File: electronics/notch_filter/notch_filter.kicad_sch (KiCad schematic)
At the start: 32 parts, among them J1 Conn_01x03, J2 Conn_01x03, J3 Output, J4 In, J5 module_2x15_left_input, J6 module_2x15_right_input, U1 opamp_single_8pin

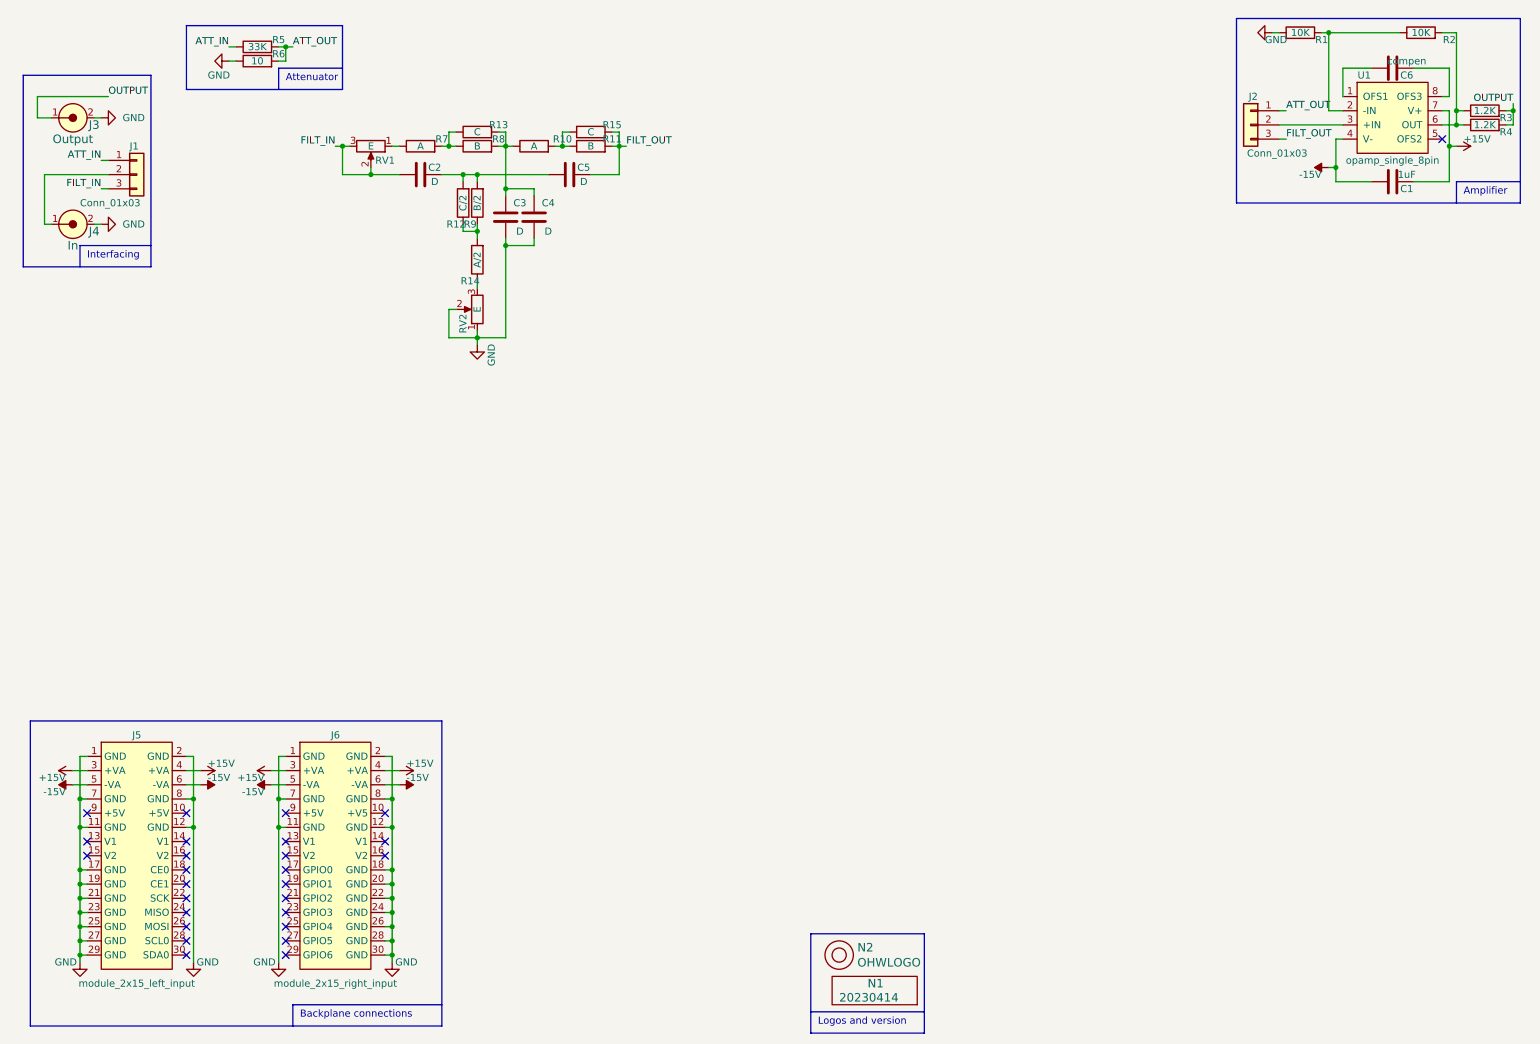
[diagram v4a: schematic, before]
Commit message: footprint changes, changed power rails, silk placed, added labels, increased size of labels
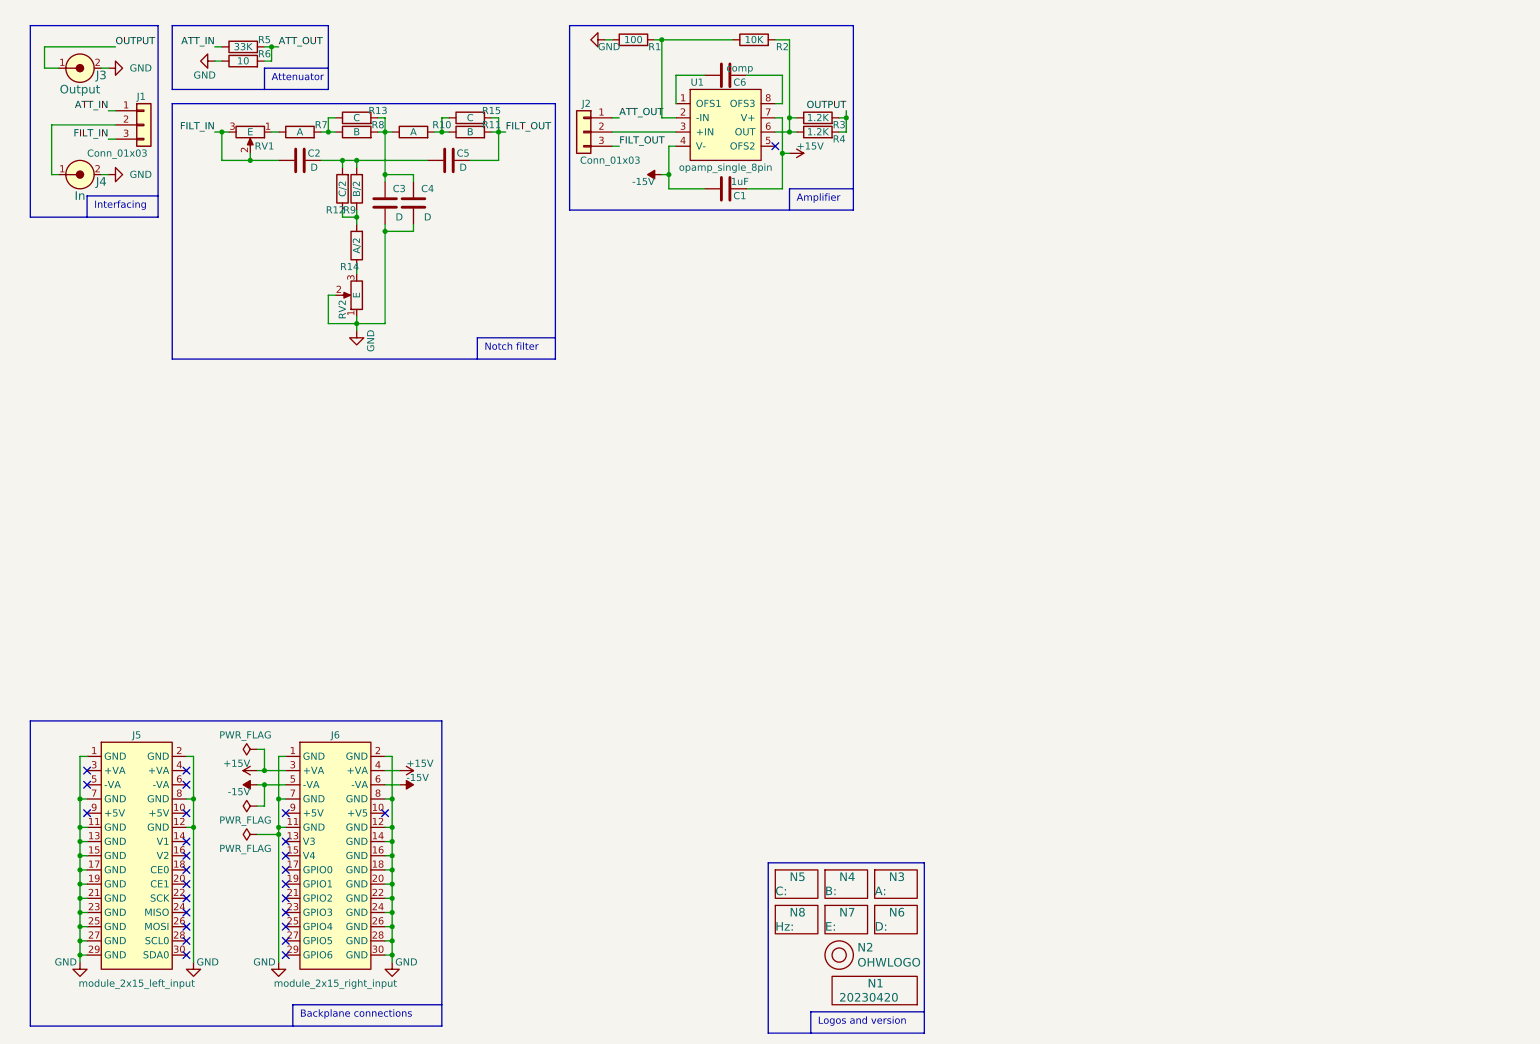
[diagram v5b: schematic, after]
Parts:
- added N3: A:, SquantorLabels:Label_Note_medium, symbol SquantorLabels:Label
- added N4: B:, SquantorLabels:Label_Note_medium, symbol SquantorLabels:Label
- added N5: C:, SquantorLabels:Label_Note_medium, symbol SquantorLabels:Label
- added N6: D:, SquantorLabels:Label_Note_medium, symbol SquantorLabels:Label
- added N7: E:, SquantorLabels:Label_Note_medium, symbol SquantorLabels:Label
- added N8: Hz:, SquantorLabels:Label_Note_medium, symbol SquantorLabels:Label
- C2, C3, C4, C5: footprint SquantorRcl:C-025_050-050X100-film -> SquantorRcl:C-025_050-050X100-0805-3516-film
- C6: value compen -> comp
- N1: value 20230414 -> 20230420
- R1: value 10K -> 100
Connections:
- net +15V: no longer J5.3 (+VA), J5.4 (+VA)
- net -15V: no longer J5.5 (-VA), J5.6 (-VA)
- net GND: now also J5.13 (GND), J5.15 (GND), J6.14 (GND), J6.16 (GND)
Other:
- note added: "Notch filter"
- moved on the sheet: C1, C2, C3, C4, C5, C6, J1, J2, J3, J4, R1, R10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

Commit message: added 1M input resistor
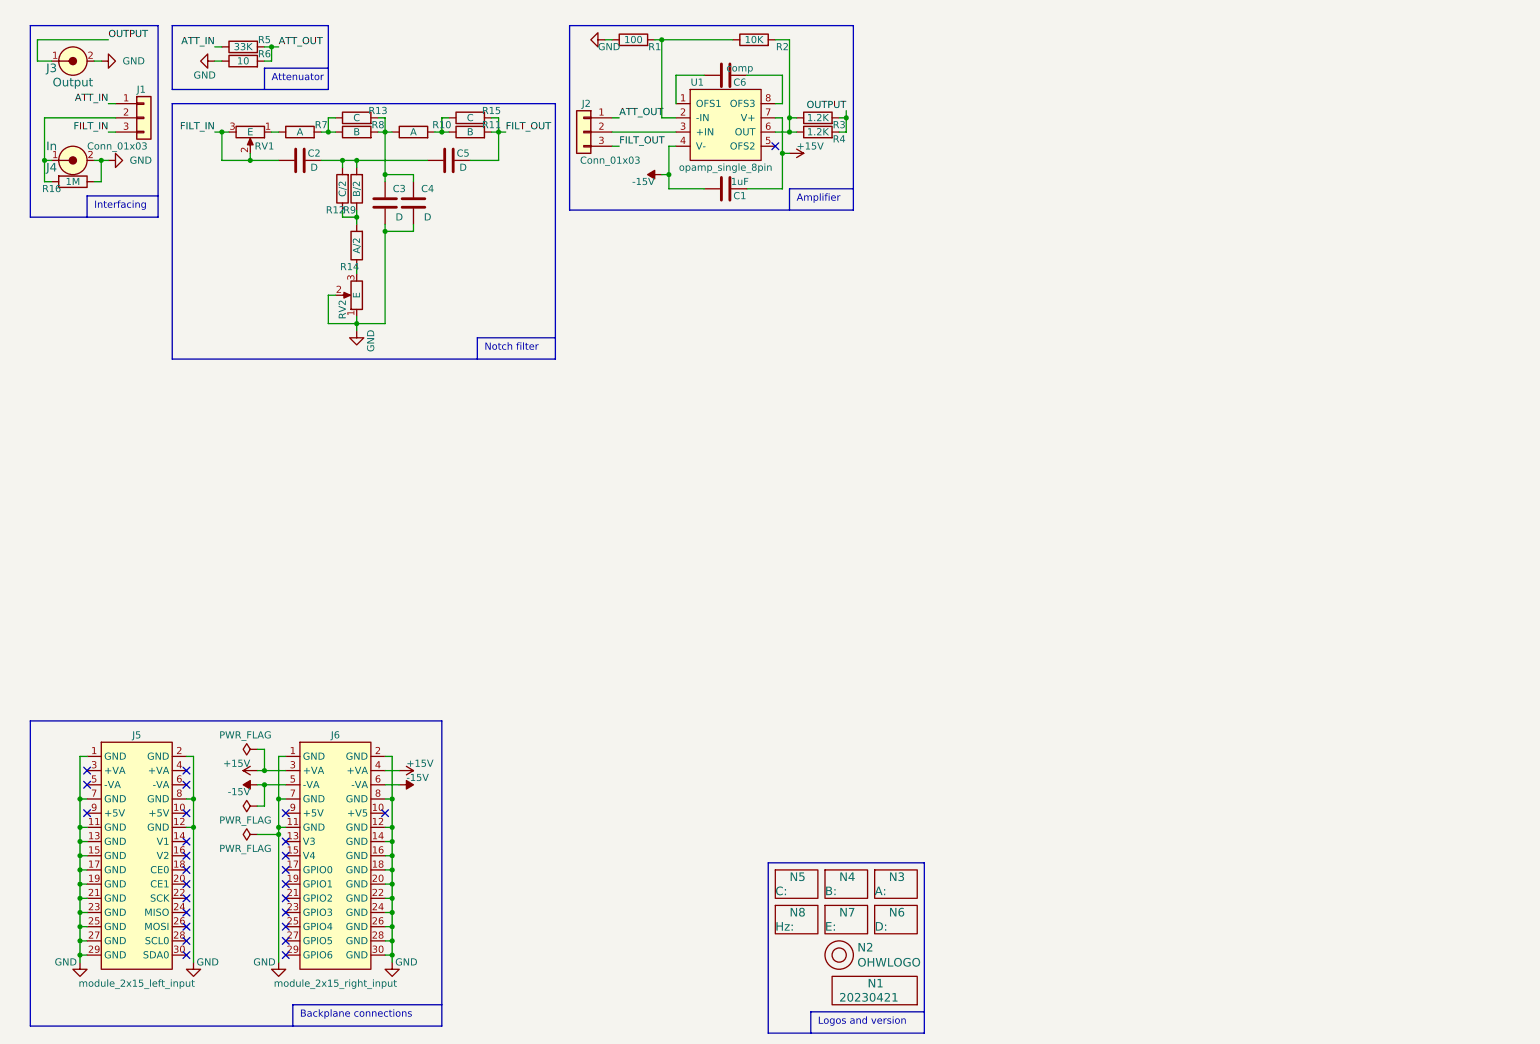
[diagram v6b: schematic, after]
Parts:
- added R16: 1M, SquantorRcl:R_0805+0603, symbol Device:R
- N1: value 20230420 -> 20230421
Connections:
- net GND: now also R16.1
- net at J1.2 (Pin_2), J4.1: now also R16.2
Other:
- moved on the sheet: J1, J3, J4

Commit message: ERC/DRC passes, small ergonomic changes
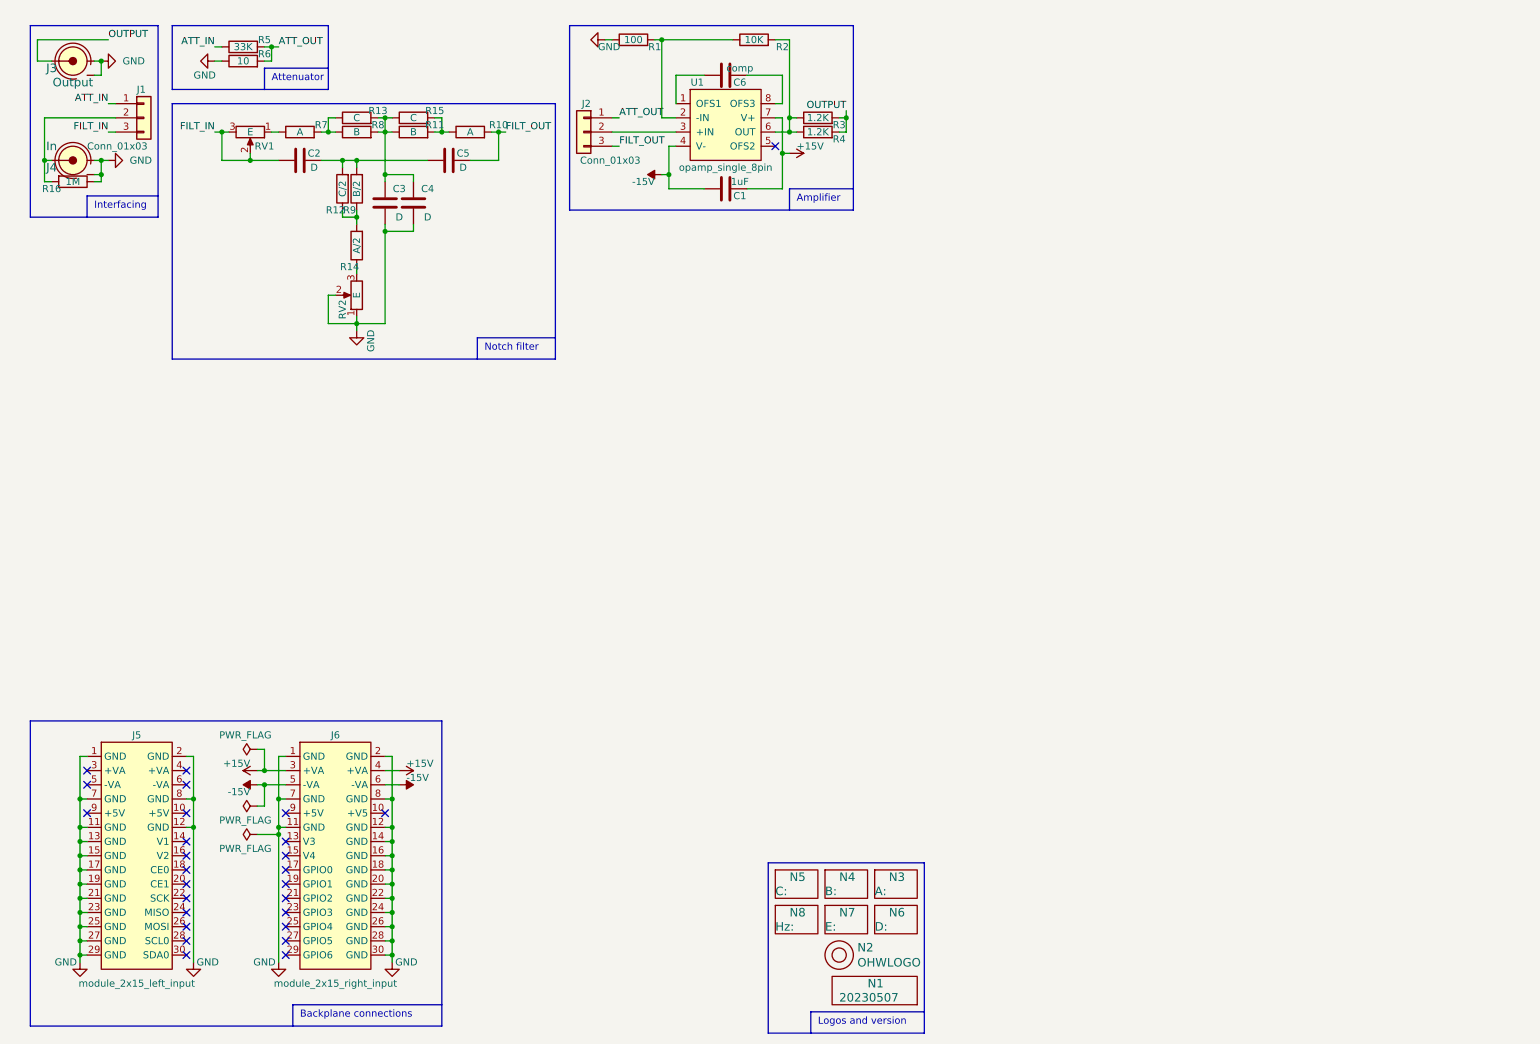
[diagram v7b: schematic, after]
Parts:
- J3, J4: symbol SquantorConnectors:Coax -> SquantorConnectors:Coax_shielded
- N1: value 20230421 -> 20230507
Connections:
- net FILT_OUT: now also R10.2; no longer R11.2, R15.2
- net GND: now also J3.S, J4.S
- net at C3.2, C4.2, R13.2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: now also R11.1, R15.1; no longer R10.1
- new net: R10.1, R11.2, R15.2
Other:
- moved on the sheet: R10, R11, R15
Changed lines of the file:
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@@
   (junction (at 24.13 179.07) (diameter 0) (color 0 0 0 0)
   )
+  (junction (at 78.74 31.75) (diameter 0) (color 0 0 0 0)
+  )
   (junction (at 80.01 181.61) (diameter 0) (color 0 0 0 0)
   )
@@
   (junction (at 17.78 39.37) (diameter 0) (color 0 0 0 0)
   )
+  (junction (at 27.94 41.91) (diameter 0) (color 0 0 0 0)
+  )
   (junction (at 24.13 161.29) (diameter 0) (color 0 0 0 0)
   )
@@
   )
   (junction (at 73.66 68.58) (diameter 0) (color 0 0 0 0)
+  )
+  (junction (at 27.94 21.59) (diameter 0) (color 0 0 0 0)
   )
   (junction (at 68.58 34.29) (diameter 0) (color 0 0 0 0)
@@
     (stroke (width 0) (type default) (color 0 0 0 0))
   )
+  (wire (pts (xy 27.94 21.59) (xy 27.94 24.13))
+    (stroke (width 0) (type default) (color 0 0 0 0))
+  )
   (wire (pts (xy 59.69 153.67) (xy 60.96 153.67))
     (stroke (width 0) (type default) (color 0 0 0 0))
@@
     (stroke (width 0) (type default) (color 0 0 0 0))
   )
-  (wire (pts (xy 27.94 43.18) (xy 27.94 39.37))
+  (wire (pts (xy 27.94 43.18) (xy 27.94 41.91))
     (stroke (width 0) (type default) (color 0 0 0 0))
   )
@@
     (stroke (width 0) (type default) (color 0 0 0 0))
   )
-  (wire (pts (xy 99.06 31.75) (xy 99.06 34.29))
-    (stroke (width 0) (type default) (color 0 0 0 0))
-  )
   (polyline (pts (xy 162.56 15.24) (xy 111.76 15.24))
     (stroke (width 0) (type default) (color 0 0 0 0))
@@
     (stroke (width 0) (type default) (color 0 0 0 0))
   )
+  (wire (pts (xy 78.74 31.75) (xy 80.01 31.75))
+    (stroke (width 0) (type default) (color 0 0 0 0))
+  )
   (wire (pts (xy 83.82 41.91) (xy 78.74 41.91))
     (stroke (width 0) (type default) (color 0 0 0 0))
@@
     (stroke (width 0) (type default) (color 0 0 0 0))
   )
-  (wire (pts (xy 90.17 31.75) (xy 88.9 31.75))
+  (wire (pts (xy 87.63 31.75) (xy 88.9 31.75))
     (stroke (width 0) (type default) (color 0 0 0 0))
   )
@@
     (stroke (width 0) (type default) (color 0 0 0 0))
   )
-  (wire (pts (xy 97.79 31.75) (xy 99.06 31.75))
-    (stroke (width 0) (type default) (color 0 0 0 0))
-  )
   (wire (pts (xy 80.01 168.91) (xy 80.01 171.45))
     (stroke (width 0) (type default) (color 0 0 0 0))
@@
     (stroke (width 0) (type default) (color 0 0 0 0))
   )
+  (wire (pts (xy 27.94 41.91) (xy 27.94 39.37))
+    (stroke (width 0) (type default) (color 0 0 0 0))
+  )
   (wire (pts (xy 97.79 34.29) (xy 99.06 34.29))
     (stroke (width 0) (type default) (color 0 0 0 0))
@@
     (stroke (width 0) (type default) (color 0 0 0 0))
   )
+  (wire (pts (xy 27.94 24.13) (xy 26.67 24.13))
+    (stroke (width 0) (type default) (color 0 0 0 0))
+  )
   (wire (pts (xy 49.53 39.37) (xy 49.53 34.29))
     (stroke (width 0) (type default) (color 0 0 0 0))
@@
   )
   (wire (pts (xy 24.13 173.99) (xy 24.13 176.53))
+    (stroke (width 0) (type default) (color 0 0 0 0))
+  )
+  (wire (pts (xy 26.67 41.91) (xy 27.94 41.91))
     (stroke (width 0) (type default) (color 0 0 0 0))
   )
@@
       (effects (font (size 1.524 1.524)) (justify left))
     )
-    (property "Value" "20230421" (id 1) (at 160.02 189.23 0)
+    (property "Value" "20230507" (id 1) (at 160.02 189.23 0)
       (effects (font (size 1.524 1.524)) (justify left))
     )
@@
     (pin "2")
   )
-  (symbol (lib_id "Device:R") (at 93.98 34.29 90) (unit 1)
-    (in_bom yes) (on_board yes)
-    (property "Reference" "R11" (id 0) (at 97.79 33.02 90))
-    (property "Value" "B" (id 1) (at 93.98 34.29 90))
-    (property "Footprint" "SquantorRcl:R_0805+0603" (id 2) (at 93.98 36.068 90)
-      (effects (font (size 1.27 1.27)) hide)
-    )
-    (property "Datasheet" "~" (id 3) (at 93.98 34.29 0)
+  (symbol (lib_id "Device:R") (at 83.82 34.29 90) (unit 1)
+    (in_bom yes) (on_board yes)
+    (property "Reference" "R11" (id 0) (at 87.63 33.02 90))
+    (property "Value" "B" (id 1) (at 83.82 34.29 90))
+    (property "Footprint" "SquantorRcl:R_0805+0603" (id 2) (at 83.82 36.068 90)
+      (effects (font (size 1.27 1.27)) hide)
+    )
+    (property "Datasheet" "~" (id 3) (at 83.82 34.29 0)
       (effects (font (size 1.27 1.27)) hide)
     )
@@
     (pin "2")
   )
-  (symbol (lib_id "SquantorConnectors:Coax") (at 22.86 21.59 0) (unit 1)
+  (symbol (lib_id "SquantorConnectors:Coax_shielded") (at 22.86 21.59 0) (unit 1)
     (in_bom yes) (on_board yes)
     (property "Reference" "J3" (id 0) (at 19.05 22.86 0)
@@
     (pin "1")
     (pin "2")
-  )
-  (symbol (lib_id "Device:R") (at 83.82 34.29 90) (unit 1)
-    (in_bom yes) (on_board yes)
-    (property "Reference" "R10" (id 0) (at 88.9 33.02 90))
-    (property "Value" "A" (id 1) (at 83.82 34.29 90))
-    (property "Footprint" "SquantorRcl:R_0805+0603" (id 2) (at 83.82 36.068 90)
-      (effects (font (size 1.27 1.27)) hide)
-    )
-    (property "Datasheet" "~" (id 3) (at 83.82 34.29 0)
+    (pin "S")
+  )
+  (symbol (lib_id "Device:R") (at 93.98 34.29 90) (unit 1)
+    (in_bom yes) (on_board yes)
+    (property "Reference" "R10" (id 0) (at 99.06 33.02 90))
+    (property "Value" "A" (id 1) (at 93.98 34.29 90))
+    (property "Footprint" "SquantorRcl:R_0805+0603" (id 2) (at 93.98 36.068 90)
+      (effects (font (size 1.27 1.27)) hide)
+    )
+    (property "Datasheet" "~" (id 3) (at 93.98 34.29 0)
       (effects (font (size 1.27 1.27)) hide)
     )
@@
     (pin "1")
   )
-  (symbol (lib_id "Device:R") (at 93.98 31.75 90) (unit 1)
-    (in_bom yes) (on_board yes)
-    (property "Reference" "R15" (id 0) (at 97.79 30.48 90))
-    (property "Value" "C" (id 1) (at 93.98 31.75 90))
-    (property "Footprint" "SquantorRcl:R_0805+0603" (id 2) (at 93.98 33.528 90)
-      (effects (font (size 1.27 1.27)) hide)
-    )
-    (property "Datasheet" "~" (id 3) (at 93.98 31.75 0)
+  (symbol (lib_id "Device:R") (at 83.82 31.75 90) (unit 1)
+    (in_bom yes) (on_board yes)
+    (property "Reference" "R15" (id 0) (at 87.63 30.48 90))
+    (property "Value" "C" (id 1) (at 83.82 31.75 90))
+    (property "Footprint" "SquantorRcl:R_0805+0603" (id 2) (at 83.82 33.528 90)
+      (effects (font (size 1.27 1.27)) hide)
+    )
+    (property "Datasheet" "~" (id 3) (at 83.82 31.75 0)
       (effects (font (size 1.27 1.27)) hide)
     )
@@
     (pin "3")
   )
-  (symbol (lib_id "SquantorConnectors:Coax") (at 22.86 39.37 0) (unit 1)
+  (symbol (lib_id "SquantorConnectors:Coax_shielded") (at 22.86 39.37 0) (unit 1)
     (in_bom yes) (on_board yes)
     (property "Reference" "J4" (id 0) (at 19.05 40.64 0)
@@
     (pin "1")
     (pin "2")
+    (pin "S")
   )
   (symbol (lib_id "SquantorLabels:Label") (at 161.29 168.91 0) (unit 1)
@@
     )
     (path "/00000000-0000-0000-0000-00005ee12bf3"
-      (reference "N1") (unit 1) (value "20230421") (footprint "SquantorLabels:Label_Generic")
+      (reference "N1") (unit 1) (value "20230507") (footprint "SquantorLabels:Label_Generic")
     )
     (path "/00000000-0000-0000-0000-00005ee13678"
